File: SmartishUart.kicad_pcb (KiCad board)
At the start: 2 copper layers, 19 x 59.8 mm, 29 parts, among them J1 USB_C_Receptacle_USB2.0, J2 UART, J3 V_SEL, J4 Conn_01x07, J5 PROG_SEL, J6 RESET_SEL, Q1 MMBT2222, Q2 MMBT2222, SW1 TL3342, SW2 TL3342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

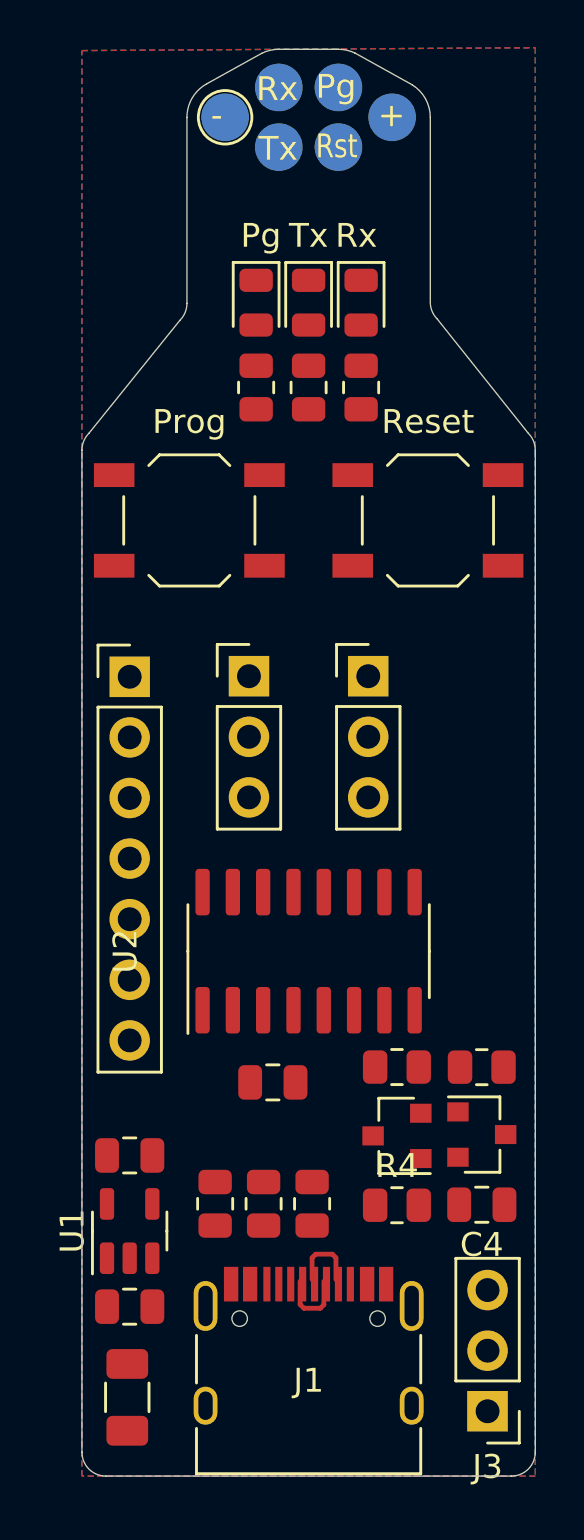
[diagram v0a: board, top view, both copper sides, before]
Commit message: Various updates
- Added LED to all output pins
- Dropped pogopin area
- Made 'CTS' pin configurable
- Added lots of lables
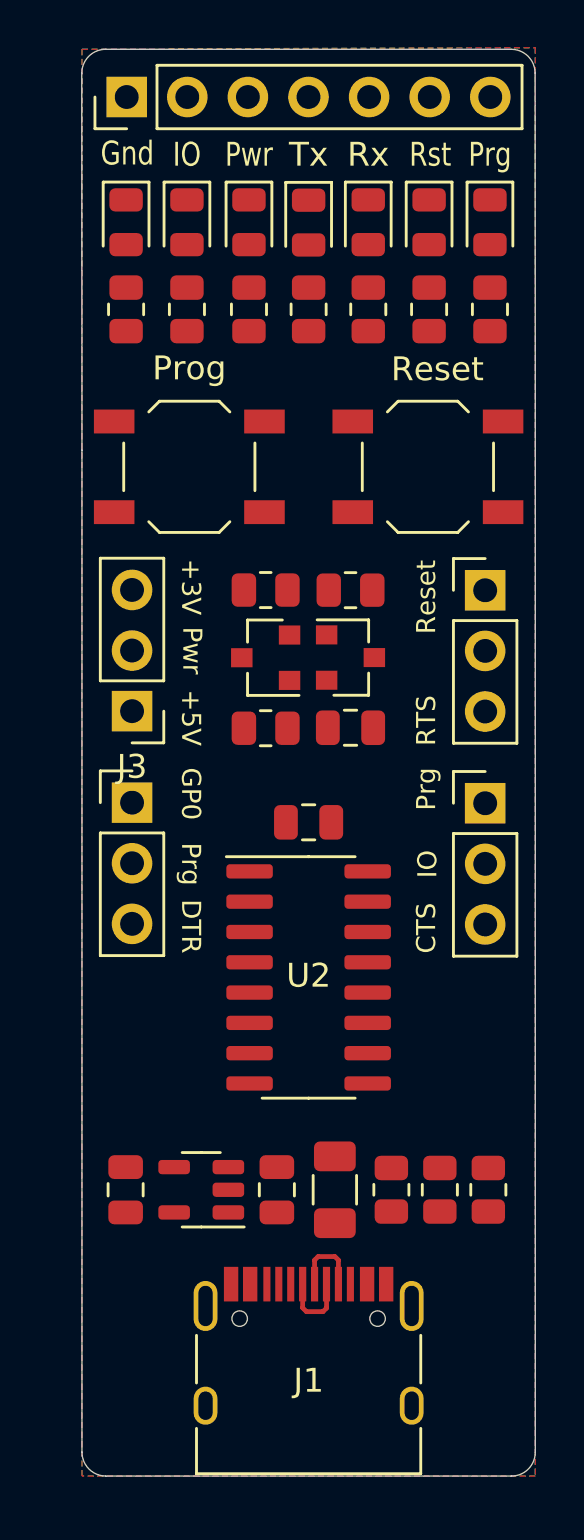
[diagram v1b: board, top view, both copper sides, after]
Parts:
- removed J2: UART, SmartishUart:Prog_1
- added D4: LED, LED_SMD:LED_0805_2012Metric, F.Cu at (149.5, 63.5)
- added D5: LED, LED_SMD:LED_0805_2012Metric, F.Cu at (157.1, 63.5)
- added D6: LED, LED_SMD:LED_0805_2012Metric, F.Cu at (144.3, 63.5)
- added D7: LED, LED_SMD:LED_0805_2012Metric, F.Cu at (146.9, 63.5)
- added J7: PROG_SEL, Connector_PinHeader_2.54mm:PinHeader_1x03_P2.54mm_Vertical, F.Cu at (159.4, 87.8)
- added R10: 1K, Resistor_SMD:R_0805_2012Metric, F.Cu at (149.5, 67.1)
- added R11: 1K, Resistor_SMD:R_0805_2012Metric, F.Cu at (157.1, 67.1)
- added R12: 1K, Resistor_SMD:R_0805_2012Metric, F.Cu at (144.3, 67.1)
- added R13: 1K, Resistor_SMD:R_0805_2012Metric, F.Cu at (146.9, 67.1)
- moved J3 32.9 mm to (144.6, 83.9)
- moved J4 24.3 mm to (144.4, 58.2), turned to 90 degrees
- moved Q1 20.8 mm to (150.2, 81.7)
- moved Q2 20.7 mm to (153.8, 81.7)
- moved R5 20.7 mm to (150.2, 78.9)
- moved C4 20.7 mm to (153.8, 84.6)
- moved R4 20.7 mm to (150.2, 84.7)
- moved R6 20.7 mm to (153.8, 78.9)
- moved F1 12.3 mm to (153.1, 104.0)
- moved C3 11.0 mm to (152.0, 88.6)
- moved D3 10.4 mm to (159.6, 63.5)
- moved R9 10.3 mm to (159.6, 67.1)
- moved C1 7.88 mm to (150.7, 104.0), turned to 90 degrees
- moved R1 7.41 mm to (159.5, 104.0)
- moved R2 7.41 mm to (155.5, 104.0)
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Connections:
- J4 pad 2: /CTS -> /CTS_OUT
- R9 pad 2: /GPIO0 -> /PROG_OUT
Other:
- outline, holes or cut-outs redrawn
- board text added: "+3V"
- board text added: "+5V"
- board text added: "CTS"
- board text added: "DTR"
- board text added: "GP0"
- board text added: "Gnd"
- board text added: "IO"
- board text added: "Prg"
- board text added: "Pwr"
- board text added: "RTS"
- board text added: "Rst"
- board text removed: "Pg"

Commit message: A few tweaks to the layout to make it look a little neater
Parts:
- moved J5 3.66 mm to (144.6, 91.4)
- moved J7 3.66 mm to (159.4, 91.5)
- moved J3 1.83 mm to (144.6, 85.8)
- moved J6 1.83 mm to (159.4, 80.7)
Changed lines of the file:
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@@
         (effects (font (size 1 1) (thickness 0.15)))
     )
-    (fp_text user "${REFERENCE}" (at 3.556 1) (layer "F.Fab")
+    (fp_text user "${REFERENCE}" (at 3.544 2.8304) (layer "F.Fab")
         (effects (font (size 0.5 0.5) (thickness 0.08)))
     )
@@
   )
   (footprint "Connector_PinHeader_2.54mm:PinHeader_1x03_P2.54mm_Vertical" (layer "F.Cu")
-    (at 144.6 87.775)
+    (at 144.6 91.435)
     (descr "Through hole straight pin header, 1x03, 2.54mm pitch, single row")
     (tags "Through hole pin header THT 1x03 2.54mm single row")
@@
   )
   (footprint "Connector_PinHeader_2.54mm:PinHeader_1x03_P2.54mm_Vertical" (layer "F.Cu")
-    (at 159.4 87.8)
+    (at 159.4 91.46)
     (descr "Through hole straight pin header, 1x03, 2.54mm pitch, single row")
     (tags "Through hole pin header THT 1x03 2.54mm single row")
@@
   )
   (footprint "Connector_PinHeader_2.54mm:PinHeader_1x03_P2.54mm_Vertical" (layer "F.Cu")
-    (at 159.4 78.875)
+    (at 159.388 80.7054)
     (descr "Through hole straight pin header, 1x03, 2.54mm pitch, single row")
     (tags "Through hole pin header THT 1x03 2.54mm single row")
@@
   )
   (footprint "Connector_PinHeader_2.54mm:PinHeader_1x03_P2.54mm_Vertical" (layer "F.Cu")
-    (at 144.6 83.94 180)
+    (at 144.588 85.7704 180)
     (descr "Through hole straight pin header, 1x03, 2.54mm pitch, single row")
     (tags "Through hole pin header THT 1x03 2.54mm single row")
@@
     (property "ki_keywords" "connector")
     (attr through_hole)
-    (fp_text reference "J3" (at 0 -2.33) (layer "F.SilkS")
+    (fp_text reference "J3" (at 0 -2.33) (layer "F.SilkS") hide
         (effects (font (size 1 1) (thickness 0.15)))
     )
@@
     (effects (font (size 1 1) (thickness 0.15)) (justify bottom))
   )
-  (gr_text "+5V" (at 146.6 85.4 270) (layer "F.SilkS")
+  (gr_text "+5V" (at 146.588 87.2304 270) (layer "F.SilkS")
     (effects (font (size 0.8 0.8) (thickness 0.15)) (justify right bottom))
   )
@@
     (effects (font (size 1 1) (thickness 0.15)) (justify bottom))
   )
-  (gr_text "DTR" (at 146.6 94.1 270) (layer "F.SilkS")
+  (gr_text "DTR" (at 146.6 97.76 270) (layer "F.SilkS")
     (effects (font (size 0.8 0.8) (thickness 0.15)) (justify right bottom))
   )
@@
     (effects (font (size 1 0.8) (thickness 0.15)) (justify bottom))
   )
-  (gr_text "Reset" (at 157.4 77.6 90) (layer "F.SilkS")
+  (gr_text "Reset" (at 157.388 79.4304 90) (layer "F.SilkS")
     (effects (font (size 0.8 0.8) (thickness 0.15)) (justify right bottom))
   )
-  (gr_text "CTS" (at 157.4 94.1 90) (layer "F.SilkS")
+  (gr_text "CTS" (at 157.4 97.76 90) (layer "F.SilkS")
     (effects (font (size 0.8 0.8) (thickness 0.15)) (justify left bottom))
   )
@@
     (effects (font (size 1 0.8) (thickness 0.15)) (justify bottom))
   )
-  (gr_text "Pwr" (at 146.65 81.4 270) (layer "F.SilkS")
+  (gr_text "Pwr" (at 146.638 83.2304 270) (layer "F.SilkS")
     (effects (font (size 0.8 0.8) (thickness 0.15)) (justify bottom))
   )
-  (gr_text "IO" (at 157.45 90.35 90) (layer "F.SilkS")
+  (gr_text "IO" (at 157.45 94.01 90) (layer "F.SilkS")
     (effects (font (size 0.8 0.8) (thickness 0.15)) (justify bottom))
   )
@@
     (effects (font (size 1 0.8) (thickness 0.15)) (justify bottom))
   )
-  (gr_text "GP0" (at 146.6 86.3 270) (layer "F.SilkS")
+  (gr_text "GP0" (at 146.6 89.96 270) (layer "F.SilkS")
     (effects (font (size 0.8 0.8) (thickness 0.15)) (justify left bottom))
   )
@@
     (effects (font (size 1 0.8) (thickness 0.15)) (justify bottom))
   )
-  (gr_text "RTS" (at 157.4 85.4 90) (layer "F.SilkS")
+  (gr_text "RTS" (at 157.388 87.2304 90) (layer "F.SilkS")
     (effects (font (size 0.8 0.8) (thickness 0.15)) (justify left bottom))
   )
-  (gr_text "+3V" (at 146.6 77.55 270) (layer "F.SilkS")
+  (gr_text "+3V" (at 146.65 79.25 270) (layer "F.SilkS")
     (effects (font (size 0.8 0.8) (thickness 0.15)) (justify left bottom))
   )
-  (gr_text "Prg" (at 157.4 86.3 90) (layer "F.SilkS")
+  (gr_text "Prg" (at 157.4 89.96 90) (layer "F.SilkS")
     (effects (font (size 0.8 0.8) (thickness 0.15)) (justify right bottom))
   )
-  (gr_text "Prg" (at 146.6 90.35 270) (layer "F.SilkS")
+  (gr_text "Prg" (at 146.6 94.01 270) (layer "F.SilkS")
     (effects (font (size 0.8 0.8) (thickness 0.15)) (justify bottom))
   )

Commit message: Initial laydown of tracks
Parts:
- moved Q2 0.36 mm to (154.1, 81.7)
- moved Q1 0.24 mm to (150.0, 81.7)
- turned R2 to 90 degrees
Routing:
- net +3V3: track 0.00 -> 92.3 mm, vias 0 -> 5
- net /PROG_OUT: track 0.00 -> 66.6 mm
- net /CTS_OUT: track 0.00 -> 46.5 mm, vias 0 -> 1
- net /RXD0: track 0.00 -> 42.7 mm
- net /GPIO0: track 0.00 -> 40.1 mm
- net /TXD0: track 0.00 -> 39.9 mm, vias 0 -> 2
- net +5V: track 0.00 -> 38.2 mm
- net /VOUT: track 0.00 -> 29.8 mm
- net /DTR: track 0.00 -> 29.5 mm
- net /RESET_OUT: track 0.00 -> 27.9 mm, vias 0 -> 1
- net /RESET: track 0.00 -> 25.8 mm
- net /RTS: track 0.00 -> 20.7 mm
- net /D-: track 0.00 -> 18.9 mm, vias 0 -> 2
- net /+5V_In: track 0.00 -> 14.1 mm
- net /D+: track 6.04 -> 19.9 mm, vias 0 -> 2
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
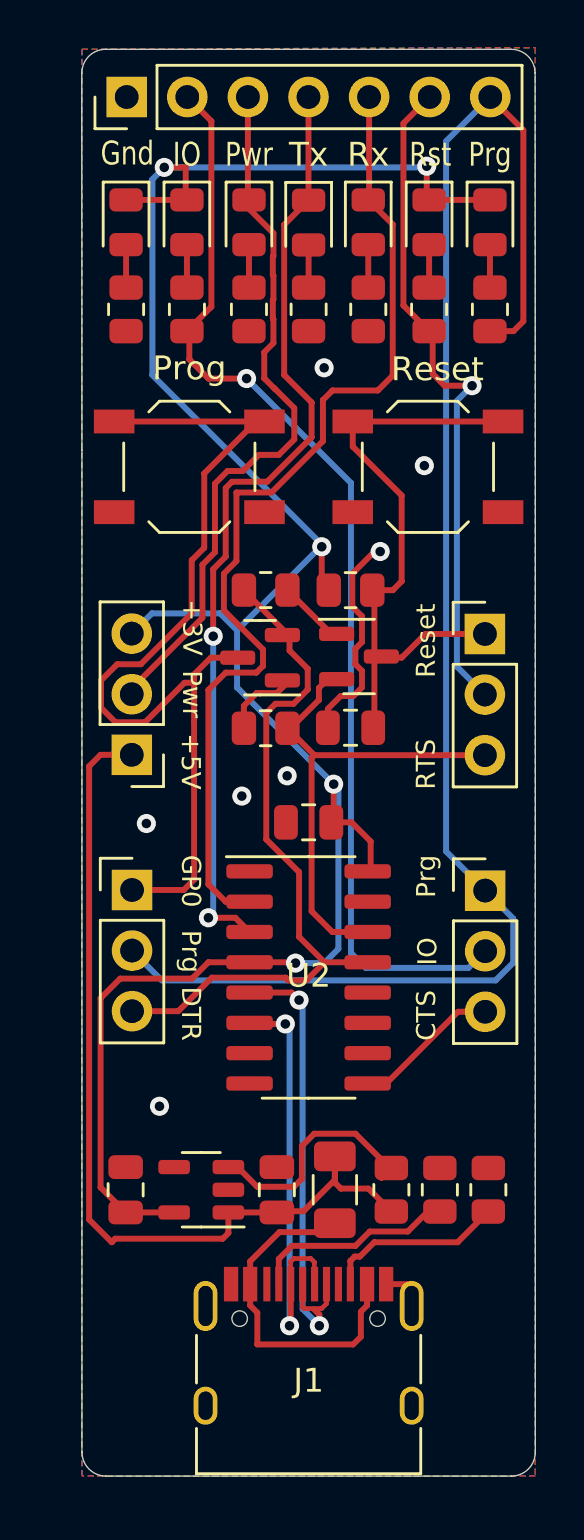
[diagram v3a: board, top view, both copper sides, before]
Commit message: Fixed the USB C connector
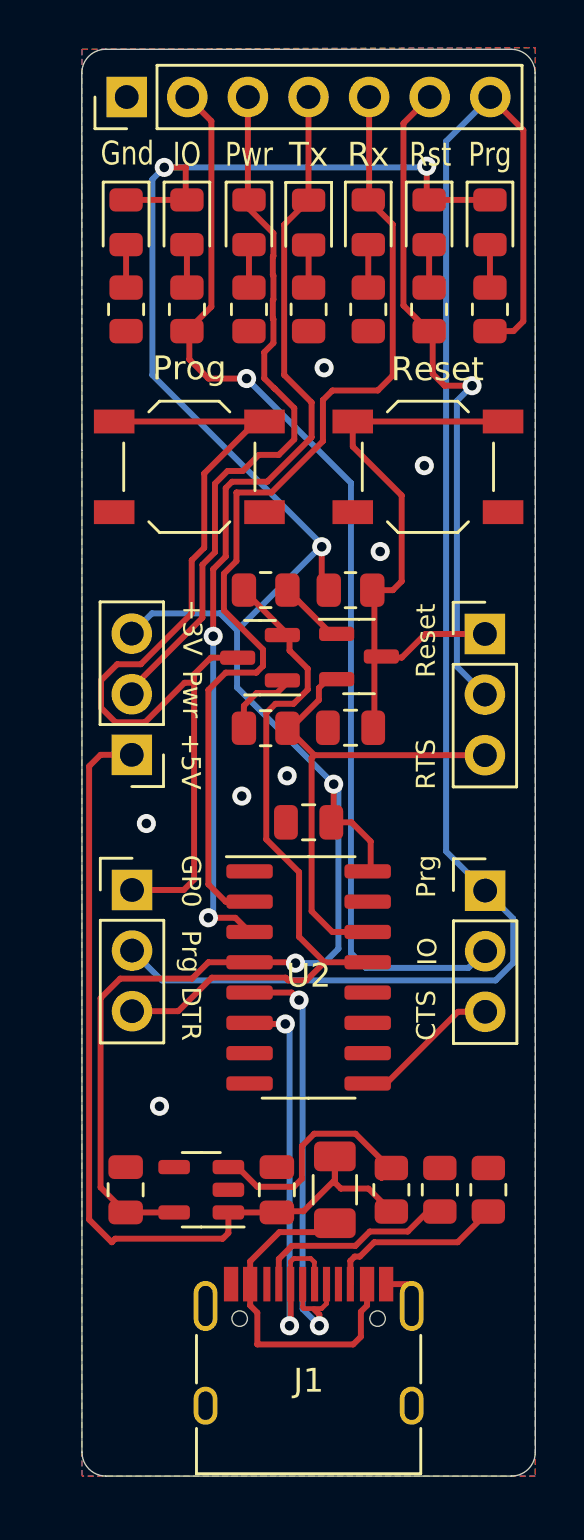
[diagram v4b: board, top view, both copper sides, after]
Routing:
- net GND: track 11.1 -> 1.15 mm
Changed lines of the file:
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@@
       (rotate (xyz 0 0 0))
+    )
+    (model "${KIPRJMOD}/HRO-TYPE-C-31-M-12.step"
+      (offset (xyz -4.5 -3.5 0))
+      (scale (xyz 1 1 1))
+      (rotate (xyz -90 0 0))
     )
   )
@@
   (segment (start 147.2 82.4) (end 147.9 81.7) (width 0.25) (layer "F.Cu") (net 10))
   (segment (start 147.625 73.975) (end 147.625 77.092239) (width 0.25) (layer "F.Cu") (net 10))
-  (segment (start 147.2 84.4) (end 147.2 82.4) (width 0.25) (layer "F.Cu") (net 10))
+  (segment (start 147.2 91) (end 147.2 82.4) (width 0.25) (layer "F.Cu") (net 10))
   (segment (start 143.3 82.65) (end 143.3 83.8) (width 0.25) (layer "F.Cu") (net 10))
-  (segment (start 147.2 91) (end 147.2 84.4) (width 0.25) (layer "F.Cu") (net 10))
   (segment (start 144.6 91.435) (end 146.765 91.435) (width 0.25) (layer "F.Cu") (net 10))
   (segment (start 152.2421 85.7854) (end 151.1125 84.6558) (width 0.25) (layer "F.Cu") (net 11))
@@
   (segment (start 150.574597 70.415072) (end 150.565415 70.415072) (width 0.25) (layer "F.Cu") (net 17))
   (segment (start 148.075 74.402208) (end 148.602208 73.875) (width 0.25) (layer "F.Cu") (net 17))
-  (segment (start 144.588 83.2304) (end 144.588 82.988497) (width 0.25) (layer "F.Cu") (net 17))
   (segment (start 150.75 73.2) (end 151.4 72.55) (width 0.25) (layer "F.Cu") (net 17))
   (segment (start 149.5 62.883166) (end 149.5 62.5125) (width 0.25) (layer "F.Cu") (net 17))
@@
   (segment (start 152.236827 101.65) (end 151.7195 102.167327) (width 0.25) (layer "F.Cu") (net 24))
   (segment (start 153.963173 101.65) (end 152.236827 101.65) (width 0.25) (layer "F.Cu") (net 24))
-  (segment (start 152.806 84.6354) (end 152.806 83.844) (width 0.25) (layer "F.Cu") (net 32))
-  (segment (start 153.881 83.303251) (end 154.2375 82.946751) (width 0.25) (layer "F.Cu") (net 32))
-  (segment (start 153.959251 81.325) (end 154.2375 81.046751) (width 0.25) (layer "F.Cu") (net 32))
-  (segment (start 156.32 107.955) (end 156.32 108.87) (width 0.25) (layer "F.Cu") (net 32))
-  (segment (start 153.831 78.181427) (end 154.762427 77.25) (width 0.25) (layer "F.Cu") (net 32))
-  (segment (start 152.806 83.844) (end 153.346749 83.303251) (width 0.25) (layer "F.Cu") (net 32))
-  (segment (start 154.2375 79.964273) (end 153.831 79.557773) (width 0.25) (layer "F.Cu") (net 32))
-  (segment (start 153.959251 81.975) (end 153.959251 81.325) (width 0.25) (layer "F.Cu") (net 32))
-  (segment (start 154.2375 81.046751) (end 154.2375 79.964273) (width 0.25) (layer "F.Cu") (net 32))
-  (segment (start 153.346749 83.303251) (end 153.881 83.303251) (width 0.25) (layer "F.Cu") (net 32))
   (segment (start 155.405 107.955) (end 156.32 107.955) (width 0.25) (layer "F.Cu") (net 32))
-  (segment (start 153.831 79.557773) (end 153.831 78.181427) (width 0.25) (layer "F.Cu") (net 32))
-  (segment (start 154.2375 82.253249) (end 153.959251 81.975) (width 0.25) (layer "F.Cu") (net 32))
   (segment (start 154.762427 77.25) (end 155 77.25) (width 0.25) (layer "F.Cu") (net 32))
-  (segment (start 154.2375 82.946751) (end 154.2375 82.253249) (width 0.25) (layer "F.Cu") (net 32))
   (via (at 152.65 69.55) (size 0.8) (drill 0.4) (layers "F.Cu" "B.Cu") (free) (net 32))
   (via (at 145.75 100.5) (size 0.8) (drill 0.4) (layers "F.Cu" "B.Cu") (free) (net 32))

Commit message: DRC error fixes
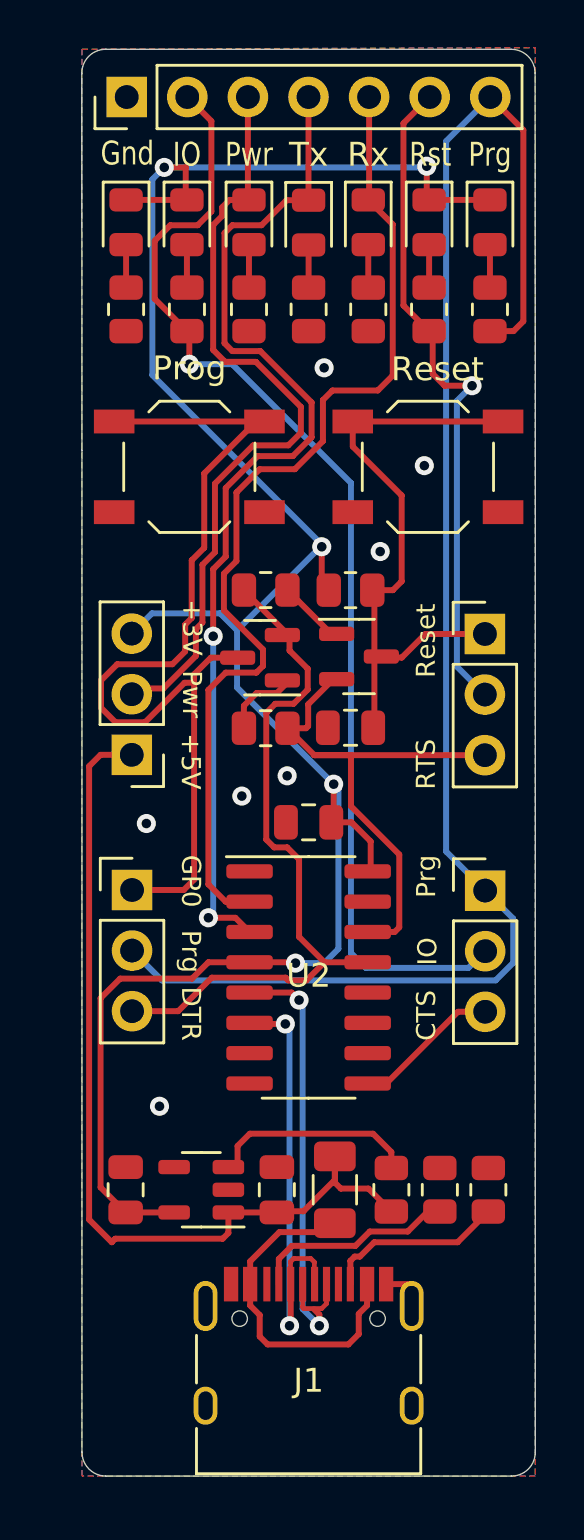
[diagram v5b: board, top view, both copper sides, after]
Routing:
- net /TXD0: track 39.9 -> 43.9 mm
- net /VOUT: track 29.6 -> 32.7 mm
- net /RTS: track 20.7 -> 23.0 mm
- net /CTS_OUT: track 46.5 -> 48.4 mm
- net Net-(U1-EN): track 9.89 -> 8.53 mm
- net /GPIO0: track 40.1 -> 40.9 mm

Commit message: Added some identification to the back of the board
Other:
- board text added: "${version_name}"
- board text added: "SmartishUART"
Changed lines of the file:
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@@
   (property "date" "2022-08-03")
   (property "version" "bd43bc3")
-  (property "version_name" "v1.1")
+  (property "version_name" "v1.0.0")
   (net 0 "")
   (net 1 "+3V3")
@@
   (gr_arc (start 143.5 116) (mid 142.794957 115.705043) (end 142.5 115)
     (stroke (width 0.05) (type default)) (layer "Edge.Cuts"))
+  (gr_text "IO" (at 146.8 61.2) (layer "B.SilkS")
+    (effects (font (size 1 0.8) (thickness 0.15)) (justify bottom mirror))
+  )
+  (gr_text "Gnd" (at 144.4 61.2) (layer "B.SilkS")
+    (effects (font (size 1 0.8) (thickness 0.15)) (justify bottom mirror))
+  )
+  (gr_text "Tx" (at 152 61.2) (layer "B.SilkS")
+    (effects (font (size 1 1) (thickness 0.15)) (justify bottom mirror))
+  )
+  (gr_text "${version_name}" (at 152 75) (layer "B.SilkS")
+    (effects (font (size 1 1) (thickness 0.15)) (justify bottom mirror))
+  )
+  (gr_text "Prg" (at 159.6 61.2) (layer "B.SilkS")
+    (effects (font (size 1 0.8) (thickness 0.15)) (justify bottom mirror))
+  )
+  (gr_text "Rx" (at 154.4 61.2) (layer "B.SilkS")
+    (effects (font (size 1 1) (thickness 0.15)) (justify bottom mirror))
+  )
+  (gr_text "Rst" (at 157 61.2) (layer "B.SilkS")
+    (effects (font (size 1 0.8) (thickness 0.15)) (justify bottom mirror))
+  )
+  (gr_text "Pwr" (at 149.4 61.2) (layer "B.SilkS")
+    (effects (font (size 1 0.8) (thickness 0.15)) (justify bottom mirror))
+  )
+  (gr_text "SmartishUART" (at 152 72.8) (layer "B.SilkS")
+    (effects (font (size 1.2 1.2) (thickness 0.2) bold) (justify bottom mirror))
+  )
   (gr_text "Reset" (at 157.4 70.1915) (layer "F.SilkS")
     (effects (font (size 1 1) (thickness 0.15)) (justify bottom))
